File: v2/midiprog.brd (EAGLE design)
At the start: 100 x 80 mm, 56 parts, among them IC1 PIC18F4550_40, IC2 TPIC6B596N, IC3 78L05Z, IC4 TPIC6B596N, Q1 8MHz, Q2 2N2222A, Q3 2N2222A, Q4 2N2222A

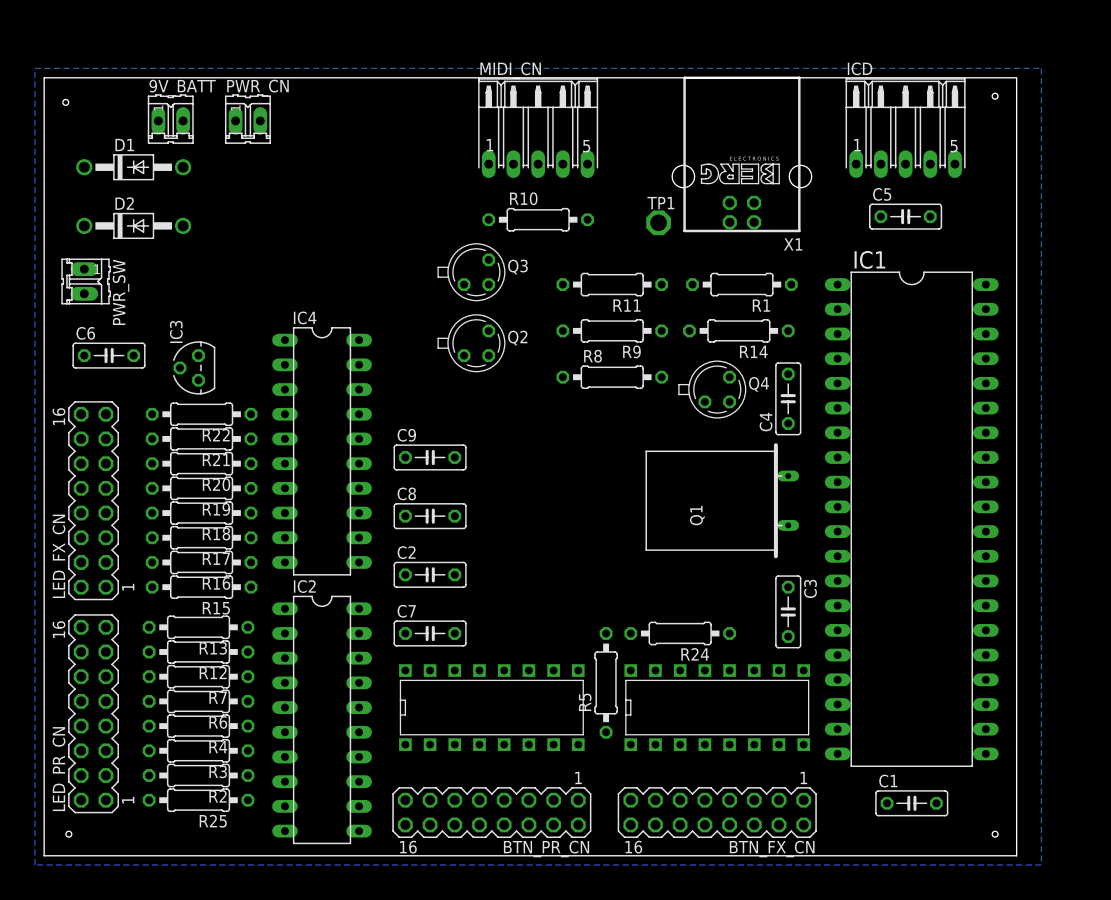
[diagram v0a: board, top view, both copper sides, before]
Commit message: An attempt at PCB routing with autorouter.
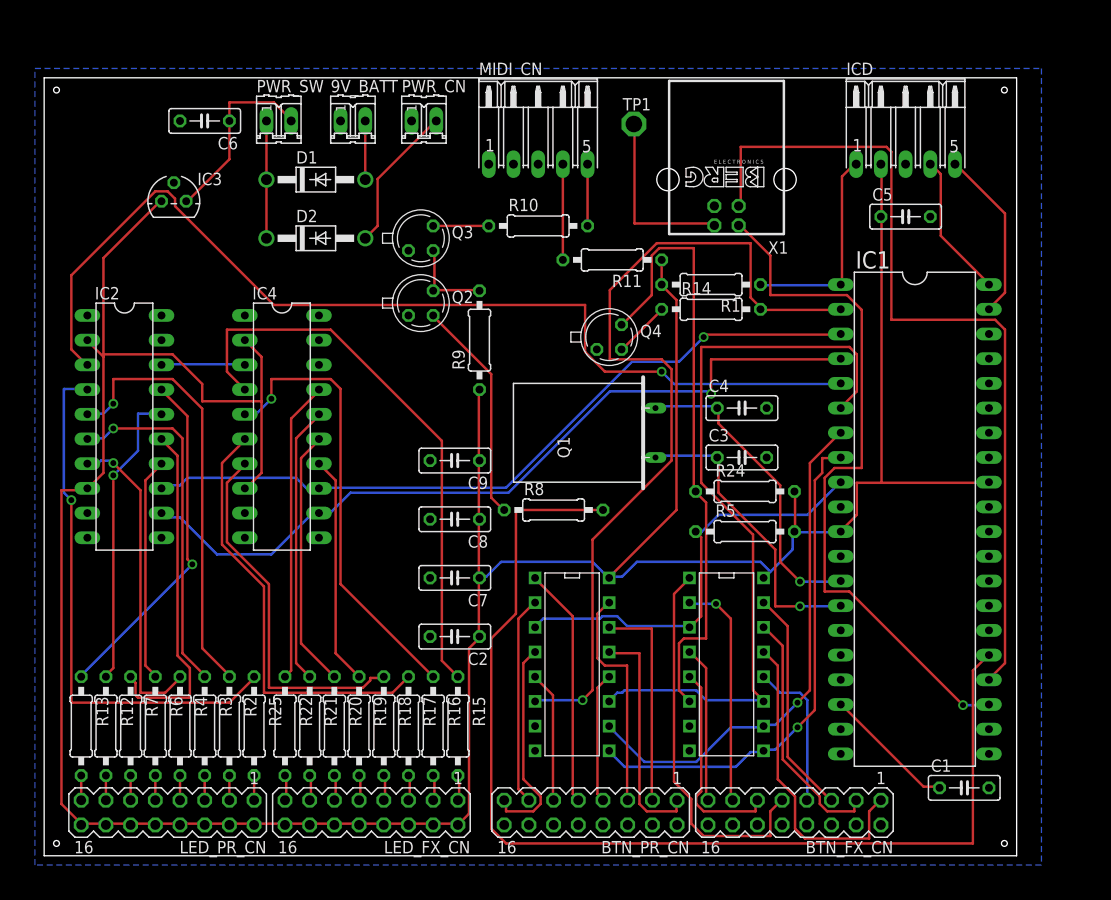
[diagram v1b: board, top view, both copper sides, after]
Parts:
- moved LED_FX_CN 43.0 mm to (33.7, 4.45), turned to 180 degrees
- moved IC2 36.4 mm to (8.26, 44.1)
- moved R22 33.2 mm to (24.8, 13.3), turned to 270 degrees
- moved R21 31.5 mm to (27.3, 13.3), turned to 270 degrees
- moved R20 30.2 mm to (29.8, 13.3), turned to 270 degrees
- moved R15 30.0 mm to (42.5, 13.3), turned to 270 degrees
- moved R19 29.3 mm to (32.4, 13.3), turned to 270 degrees
- moved R16 29.2 mm to (40.0, 13.3), turned to 270 degrees
- moved R18 28.8 mm to (34.9, 13.3), turned to 270 degrees
- moved R17 28.8 mm to (37.5, 13.3), turned to 270 degrees
- moved C6 26.1 mm to (16.5, 75.6), turned to 180 degrees
- moved PWR_SW 25.9 mm to (24.1, 75.6), turned to 0 degrees
- moved R5 21.1 mm to (72.1, 33.3), turned to 0 degrees
- moved D1 18.8 mm to (27.9, 69.5)
- moved D2 18.8 mm to (27.9, 63.5)
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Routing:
- net VDD: track 0.00 -> 331.3 mm
- net MIDI_TX: track 0.00 -> 113.0 mm
- net SHIFTREG_D: track 0.00 -> 104.1 mm, vias 0 -> 1
- net BTN_S3: track 0.00 -> 88.7 mm, vias 0 -> 1
- net USB_D+: track 0.00 -> 87.9 mm
- net SHIFTREG_RCK: track 0.00 -> 82.3 mm, vias 0 -> 1
- net BTN_S0: track 0.00 -> 78.5 mm
- net SHIFTREG_SCL: track 0.00 -> 77.6 mm, vias 0 -> 1
- net USB_D-: track 0.00 -> 72.5 mm, vias 0 -> 1
- net N$54: track 0.00 -> 63.2 mm
- net N$25: track 0.00 -> 58.7 mm
- net N$45: track 0.00 -> 55.0 mm, vias 0 -> 1
- net BTN_S1: track 0.00 -> 53.1 mm, vias 0 -> 1
- net BTN_S2: track 0.00 -> 52.4 mm, vias 0 -> 1
- net N$26: track 0.00 -> 46.5 mm, vias 0 -> 1
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
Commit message: Decent layout; not great.
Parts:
- removed R25: 220, rcl:0207/10
- added R23: 220, rcl:0207/10
- moved C5 90.0 mm to (6.35, 29.2)
- moved LED_PR_CN 62.1 mm to (5.08, 66.0), turned to 90 degrees
- moved R2 61.8 mm to (14.0, 74.9), turned to 180 degrees
- moved R3 59.1 mm to (14.0, 72.4), turned to 180 degrees
- moved IC3 57.8 mm to (71.1, 64.8)
- moved R4 56.5 mm to (14.0, 69.8), turned to 180 degrees
- moved R6 54.0 mm to (14.0, 67.3), turned to 180 degrees
- moved R7 51.7 mm to (14.0, 64.8), turned to 180 degrees
- moved C6 49.6 mm to (66.0, 72.4), turned to 270 degrees
- moved R12 49.5 mm to (14.0, 62.2), turned to 180 degrees
- moved Q4 48.8 mm to (29.2, 14.0), turned to 90 degrees
- moved LED_FX_CN 48.1 mm to (5.08, 43.2), turned to 90 degrees
- moved R15 48.1 mm to (14.0, 52.1), turned to 180 degrees
- moved R13 47.5 mm to (14.0, 59.7), turned to 180 degrees
- moved R24 45.1 mm to (27.9, 27.9), turned to 90 degrees
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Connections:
- net BFX2 renamed N$63
- net BFX4 renamed N$61
- net BFX7 renamed N$49
- net BPR2 renamed N$57
- net BPR4 renamed N$55
- net BPR7 renamed N$51
- removed net BFX1: BTN_FX_CN.1, U$2.13
- removed net BFX3: BTN_FX_CN.5, U$2.15
- removed net BFX5: BTN_FX_CN.9, U$2.1
- removed net BFX6: BTN_FX_CN.11, U$2.5
- removed net BFX8: BTN_FX_CN.15, U$2.4
- removed net BPR1: BTN_PR_CN.1, U$1.13
- removed net BPR3: BTN_PR_CN.5, U$1.15
- removed net BPR5: BTN_PR_CN.9, U$1.1
- removed net BPR6: BTN_PR_CN.11, U$1.5
- removed net BPR8: BTN_PR_CN.15, U$1.4
- removed net N$19 (its old number): LED_FX_CN.9, R19.2
- removed net N$20 (its old number): LED_FX_CN.7, R18.2
- removed net N$21 (its old number): LED_FX_CN.5, R17.2
- removed net N$22 (its old number): LED_FX_CN.3, R16.2
- removed net N$23 (its old number): LED_FX_CN.1, R15.2
- new net N$10: LED_FX_CN.11, R17.2
- new net N$13: LED_FX_CN.5, R20.2
- new net N$14: LED_FX_CN.3, R21.2
- new net N$15: LED_FX_CN.1, R22.2
- new net N$3: LED_FX_CN.13, R16.2
- new net N$46: BTN_FX_CN.9, U$2.5
- new net N$47: BTN_PR_CN.9, U$1.5
- new net N$48: BTN_FX_CN.11, U$2.4
- new net N$50: BTN_PR_CN.11, U$1.4
- new net N$52: BTN_PR_CN.15, U$1.1
- new net N$56: BTN_PR_CN.5, U$1.13
- new net N$58: BTN_PR_CN.1, U$1.15
- new net N$60: BTN_FX_CN.15, U$2.1
- new net N$62: BTN_FX_CN.5, U$2.13
- new net N$64: BTN_FX_CN.1, U$2.15
- net N$11: now also LED_FX_CN.9, R18.2; no longer LED_FX_CN.13, R21.2
- net N$12: now also LED_FX_CN.7, R19.2; no longer LED_FX_CN.11, R20.2
- net N$2: now also R15.2; no longer R22.2
- net N$24: now also R3.2; no longer R12.2
- net N$27: now also R4.2; no longer R7.2
- net N$30: now also R7.2; no longer R4.2
- net N$32: now also R12.2; no longer R3.2
- net N$36: now also R13.2; no longer R2.2
- net N$37: now also R23.2; no longer R25.2
- net N$38: now also IC2.4, R2.1; no longer IC2.17, R13.1
- net N$39: now also IC2.5, R3.1; no longer IC2.16, R12.1
- net N$40: now also IC2.6, R4.1; no longer IC2.15, R7.1
- net N$41: now also IC2.7; no longer IC2.14
- net N$42: now also IC2.14, R7.1; no longer IC2.7, R4.1
- net N$43: now also IC2.15, R12.1; no longer IC2.6, R3.1
- net N$44: now also IC2.16, R13.1; no longer IC2.5, R2.1
- net N$45: now also IC2.17, R23.1; no longer IC2.4, R25.1
- net N$6: now also R2.2; no longer R13.2
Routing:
- net MIDI_TX: track 113.0 -> 44.8 mm
- net N$54: track 63.2 -> 20.5 mm
- net BFX5: track 39.5 -> 0.00 mm
- net N$60: track 0.00 -> 37.1 mm
- net N$19: track 58.7 -> 21.9 mm
- net SHIFTREG_D: track 104.1 -> 68.2 mm
- net N$45: track 55.0 -> 21.9 mm, vias 1 -> 0
- net BFX1: track 32.0 -> 0.00 mm
- net N$52: track 0.00 -> 31.0 mm
- net N$21: track 44.4 -> 16.8 mm
- net N$20: track 46.5 -> 19.4 mm, vias 1 -> 0
- net N$44: track 44.8 -> 18.3 mm, vias 1 -> 0
- net BTN_IN: track 44.5 -> 70.5 mm
- net N$22: track 38.0 -> 13.2 mm
- net BPR5: track 24.7 -> 0.00 mm
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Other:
- board size 100 x 80 mm -> 99.1 x 78.7 mm

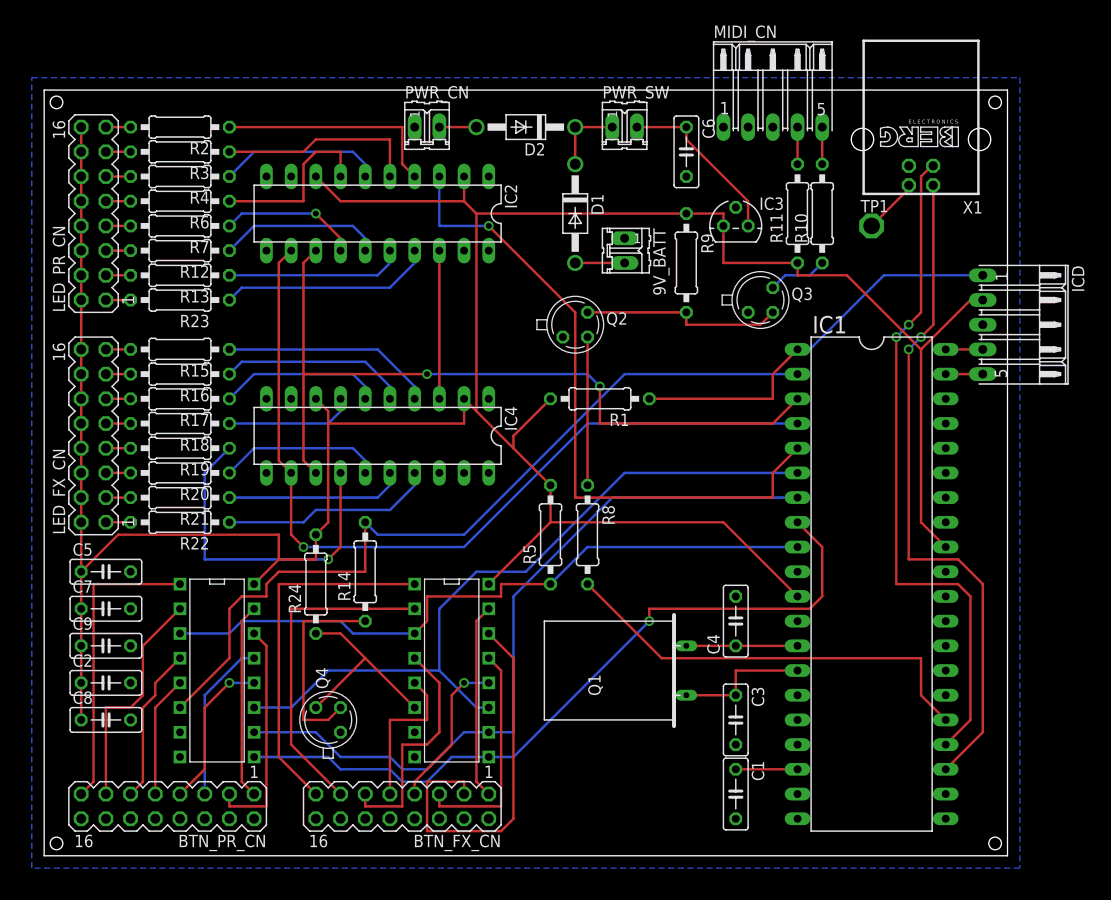
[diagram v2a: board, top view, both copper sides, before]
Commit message: Reorganized caps.
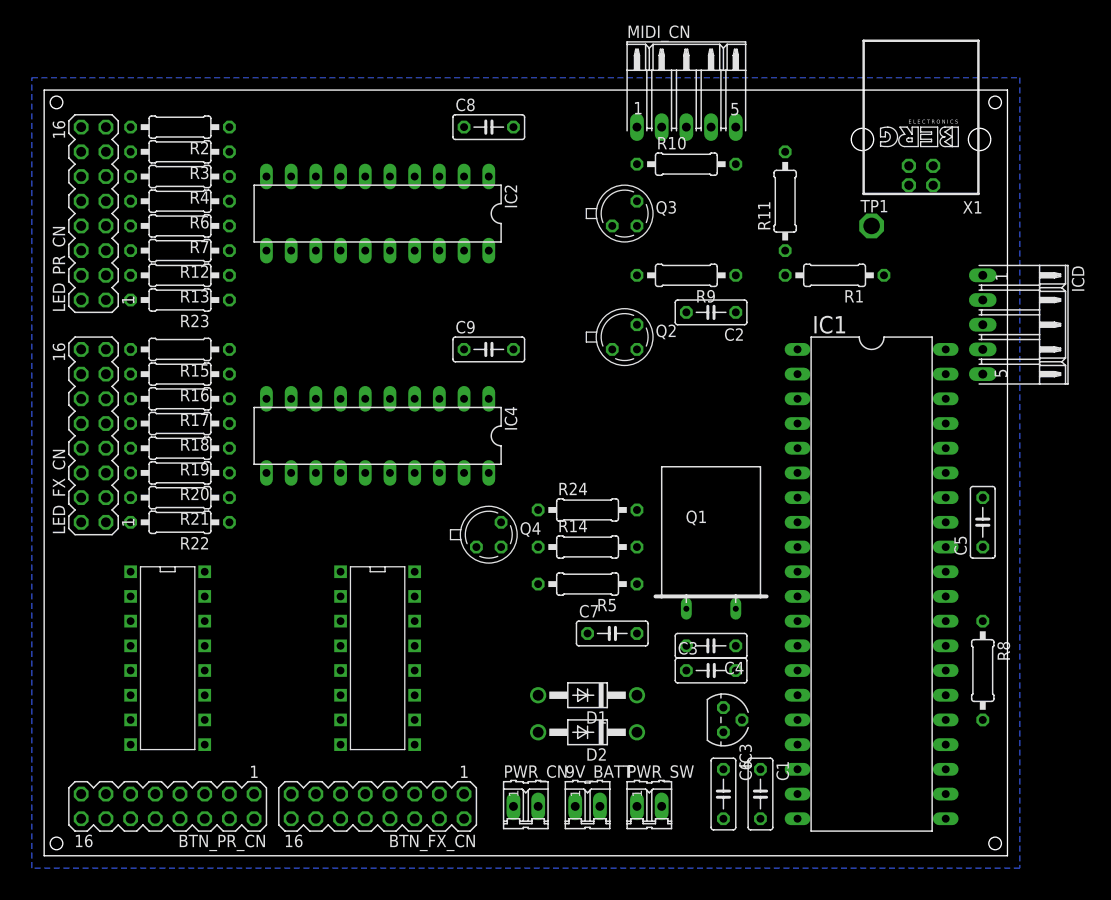
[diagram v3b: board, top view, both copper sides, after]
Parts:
- moved C5 90.3 mm to (96.5, 34.3), turned to 90 degrees
- moved C2 73.0 mm to (68.6, 55.9), turned to 180 degrees
- moved C8 72.6 mm to (45.7, 74.9)
- moved PWR_CN 70.6 mm to (49.5, 5.08)
- moved PWR_SW 69.9 mm to (62.2, 5.08)
- moved C6 66.1 mm to (69.8, 6.35)
- moved D2 62.6 mm to (55.9, 12.7)
- moved 9V_BATT 57.3 mm to (55.9, 5.08), turned to 0 degrees
- moved C7 52.1 mm to (58.4, 22.9)
- moved IC3 50.8 mm to (69.8, 14.0), turned to 270 degrees
- moved C9 49.8 mm to (45.7, 52.1)
- moved D1 49.5 mm to (55.9, 16.5), turned to 180 degrees
- moved R8 43.0 mm to (96.5, 19.1)
- moved R24 29.0 mm to (55.9, 35.6), turned to 0 degrees
- moved R1 27.3 mm to (81.3, 59.7)
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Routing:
- net VDD: track 313.5 -> 0.00 mm
- net SHIFTREG_RCK: track 88.1 -> 0.00 mm, vias 1 -> 0
- net BTN_S3: track 85.5 -> 0.00 mm
- net SHIFTREG_SCL: track 80.1 -> 0.00 mm, vias 2 -> 0
- net BTN_S1: track 77.2 -> 0.00 mm
- net BTN_S2: track 76.8 -> 0.00 mm, vias 1 -> 0
- net BTN_S0: track 76.3 -> 0.00 mm
- net BTN_IN: track 70.5 -> 0.00 mm
- net USB_D+: track 69.4 -> 0.00 mm, vias 2 -> 0
- net USB_D-: track 68.8 -> 0.00 mm, vias 2 -> 0
- net SHIFTREG_D: track 68.2 -> 0.00 mm, vias 1 -> 0
- net MIDI_TX: track 44.8 -> 0.00 mm
- net N$1: track 41.0 -> 0.00 mm
- net N$63: track 39.7 -> 0.00 mm
- net N$60: track 37.1 -> 0.00 mm
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
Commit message: Added custom package for 7805.
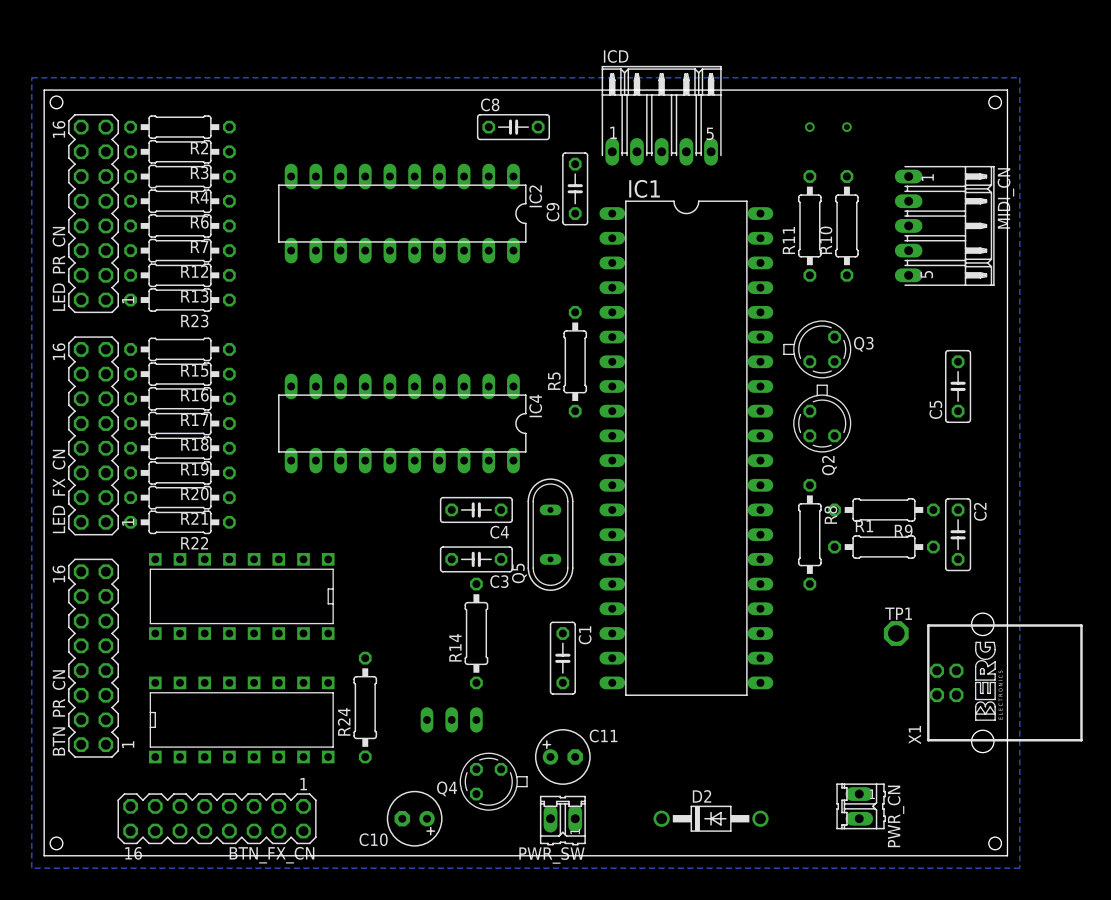
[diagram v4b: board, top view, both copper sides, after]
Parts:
- removed 9V_BATT: (no value), con-amp-quick:02P
- removed C6, C7: 10u, rcl:C050-025X075
- removed D1: 1N4001, diode:DO41-10
- removed IC3: 78L05Z, linear:TO92
- removed Q1: 8MHz, special:Q
- added C10, C11: 10u, rcl:E2,5-6
- added Q5: 8MHz, special:QS
- added U$3: 7805, 7805:JKDFJD
- moved X1 56.2 mm to (96.5, 17.8), turned to 90 degrees
- moved TP1 42.0 mm to (87.6, 22.9)
- moved ICD 37.5 mm to (63.5, 72.4), turned to 0 degrees
- moved PWR_CN 34.3 mm to (83.8, 5.08), turned to 270 degrees
- moved C2 34.2 mm to (94.0, 33.0), turned to 270 degrees
- moved R9 31.5 mm to (86.4, 35.6)
- moved R24 30.6 mm to (33.0, 15.2), turned to 90 degrees
- moved R1 28.4 mm to (86.4, 31.8), turned to 0 degrees
- moved C4 27.9 mm to (44.5, 35.6)
- moved C3 26.7 mm to (44.5, 30.5), turned to 180 degrees
- moved Q4 25.4 mm to (45.7, 7.62), turned to 180 degrees
- moved MIDI_CN 25.0 mm to (88.9, 64.8), turned to 270 degrees
- moved Q3 24.7 mm to (80.0, 52.1)
- moved C1 24.7 mm to (53.3, 20.3)
- moved IC1 23.6 mm to (66.0, 41.9)
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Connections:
- removed net N$33: 9V_BATT.2, D1.A
- net +9V: now also C10.+, U$3.1; no longer C6.1, IC3.3
- net GND: now also C10.-, C11.-, U$3.2; no longer 9V_BATT.1, C6.2, C7.2, IC3.2
- net N$35: no longer D1.C
- net OSC1: now also Q5.2; no longer Q1.2
- net OSC2: now also Q5.1; no longer Q1.1
- net VDD: now also C11.+, U$3.3; no longer C7.1, IC3.1

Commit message: Added correct parts from SparkFun to schematic and board.
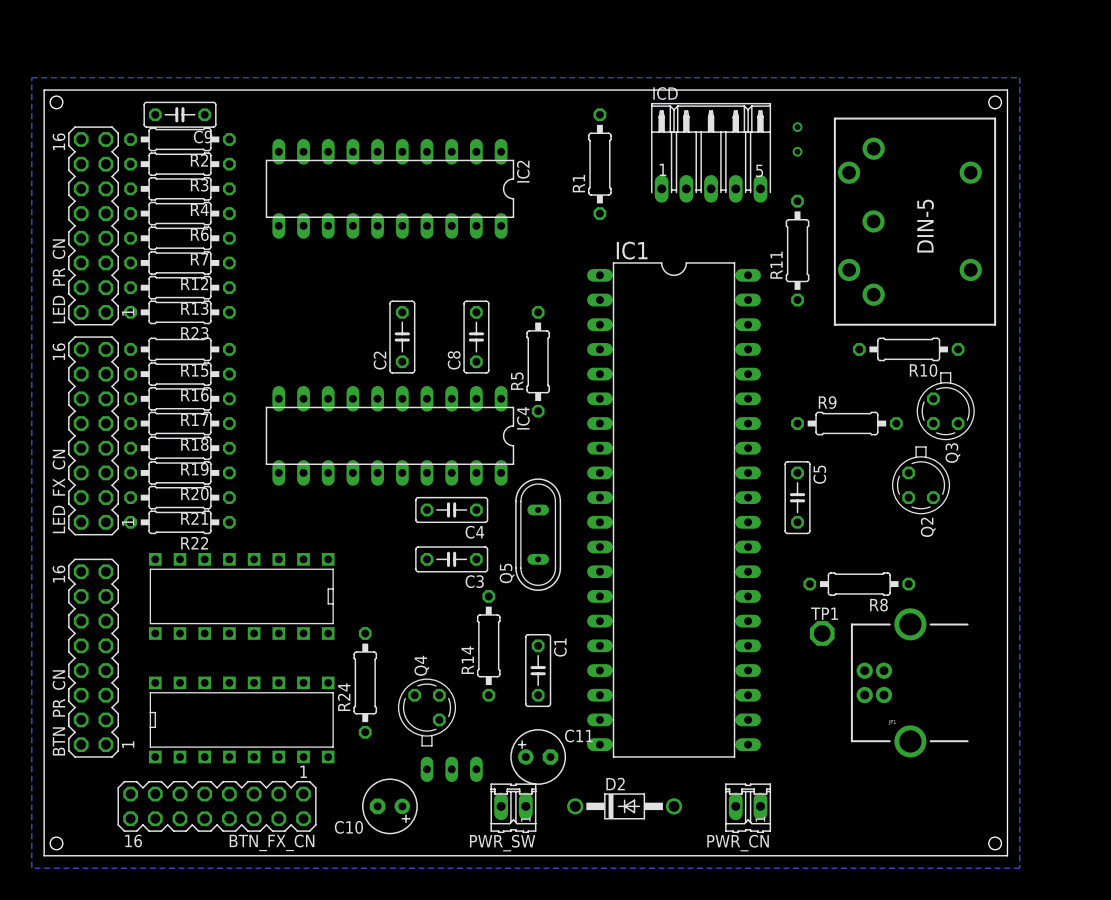
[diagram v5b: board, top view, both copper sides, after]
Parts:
- removed MIDI_CN: (no value), con-amp-quick:05PA
- removed X1: (no value), con-berg:PN61729
- added JP1: USB-B, SparkFun-Connectors-fdb4deb3ddf02d02cecaec8c0f5c972a585683b1:USB-B-PTH
- added MIDI_OUT: MIDI_CONN_FEMALE_SUPPORT, SparkFun-Connectors-fdb4deb3ddf02d02cecaec8c0f5c972a585683b1:DIN_5_FEMALE_SUPPORT
- moved C2 60.7 mm to (36.8, 53.3), turned to 90 degrees
- moved R1 49.0 mm to (57.1, 71.1), turned to 90 degrees
- moved C9 41.3 mm to (14.0, 76.2), turned to 180 degrees
- moved C8 21.9 mm to (44.5, 53.3), turned to 90 degrees
- moved C5 20.1 mm to (77.5, 36.8), turned to 270 degrees
- moved R10 14.2 mm to (88.9, 52.1), turned to 180 degrees
- moved Q3 14.2 mm to (92.7, 45.7), turned to 270 degrees
- moved Q2 12.0 mm to (90.2, 38.1)
- moved PWR_CN 11.4 mm to (72.4, 5.08), turned to 180 degrees
- moved Q4 9.92 mm to (39.4, 15.2), turned to 90 degrees
- moved R9 9.67 mm to (82.5, 44.5), turned to 0 degrees
- moved D2 8.98 mm to (59.7, 5.08)
- moved TP1 7.62 mm to (80.0, 22.9)
- moved R8 7.18 mm to (83.8, 27.9), turned to 180 degrees
- moved IC1 6.48 mm to (64.8, 35.6)
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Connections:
- net GND: now also JP1.GND, MIDI_OUT.2; no longer MIDI_CN.2, X1.4
- net N$8: now also MIDI_OUT.4; no longer MIDI_CN.5
- net N$9: now also MIDI_OUT.5; no longer MIDI_CN.4
- net USB_D+: now also JP1.D+; no longer X1.3
- net USB_D-: now also JP1.D-; no longer X1.2
- net USB_VCC: now also JP1.VBUS; no longer X1.1
